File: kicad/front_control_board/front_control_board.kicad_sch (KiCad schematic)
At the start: 66 parts, among them J1 MAIN_BOARD, J2 DISPLAY, J3 PROG, J4 I2C, J5 AUX, J6 LED_OUT, Q1 DMN63D8LW, SW1 PEC11R-4215K-S0024, SW2 BTN1, SW3 BTN4, SW4 BTN2, SW5 BTN3, U1 ESP32-WROOM-32UE, U2 TCA9534

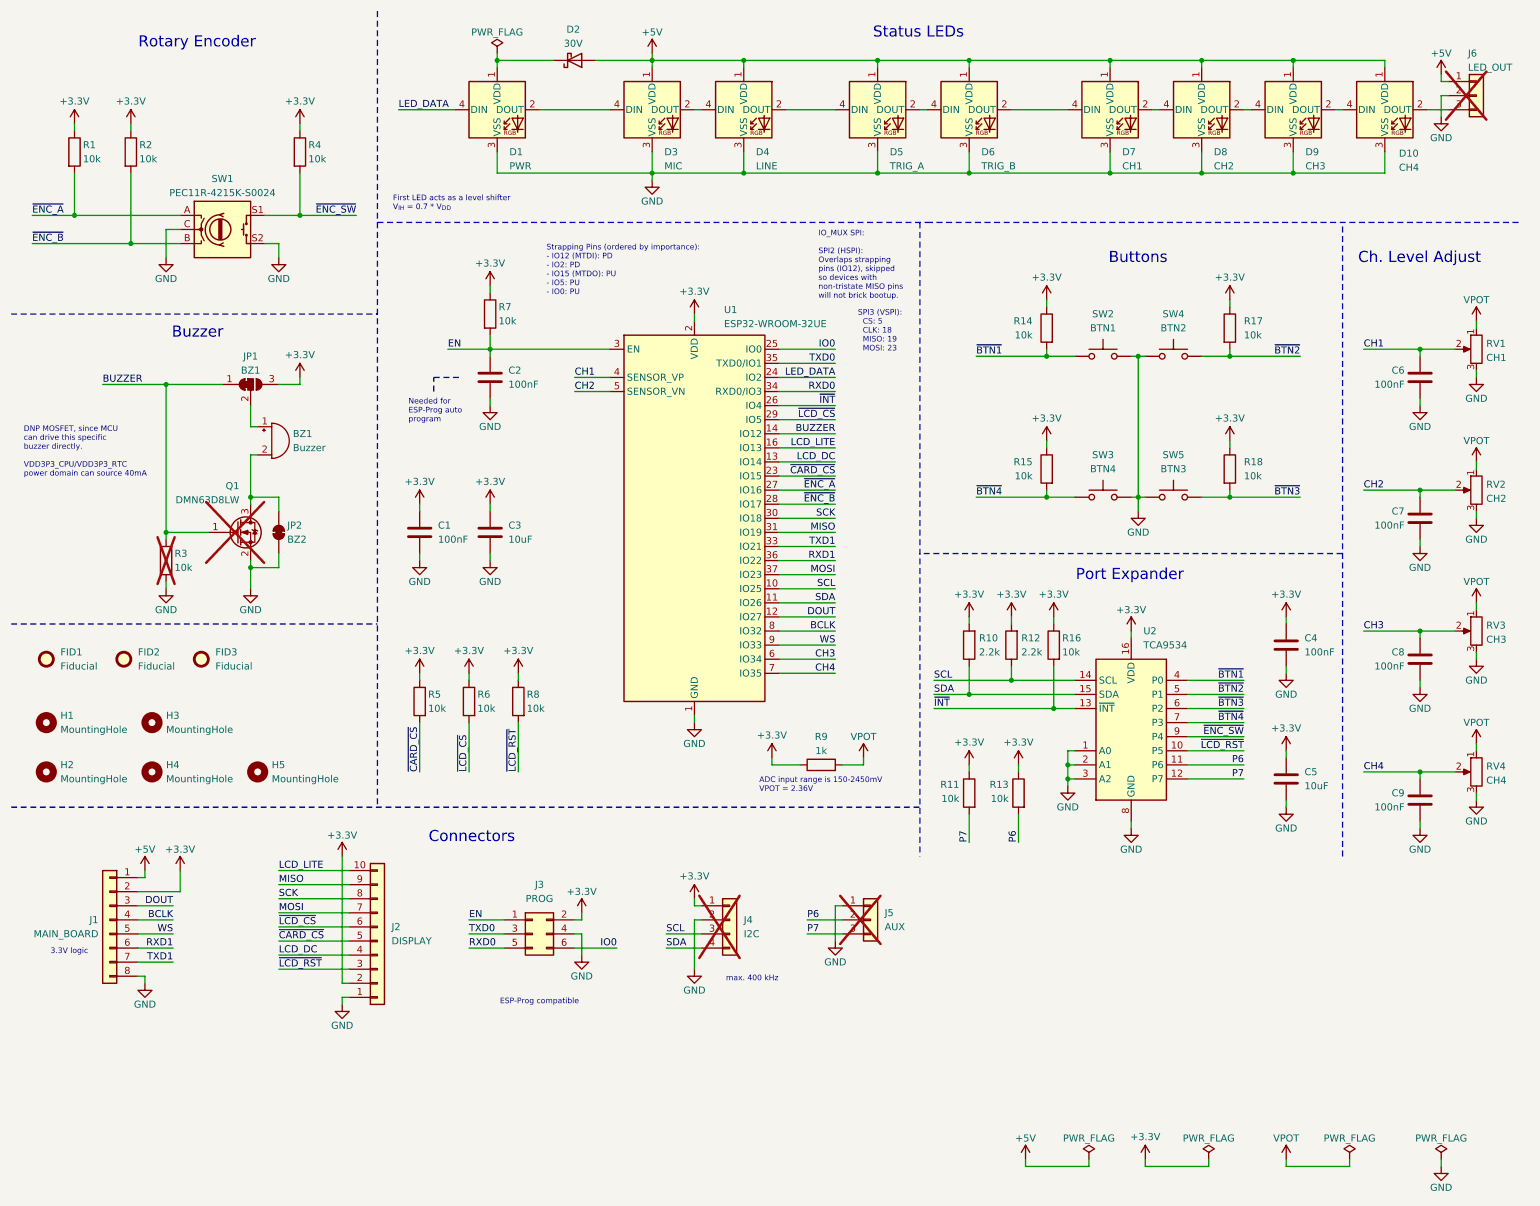
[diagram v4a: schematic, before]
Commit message: update BOM prioritizing basic parts
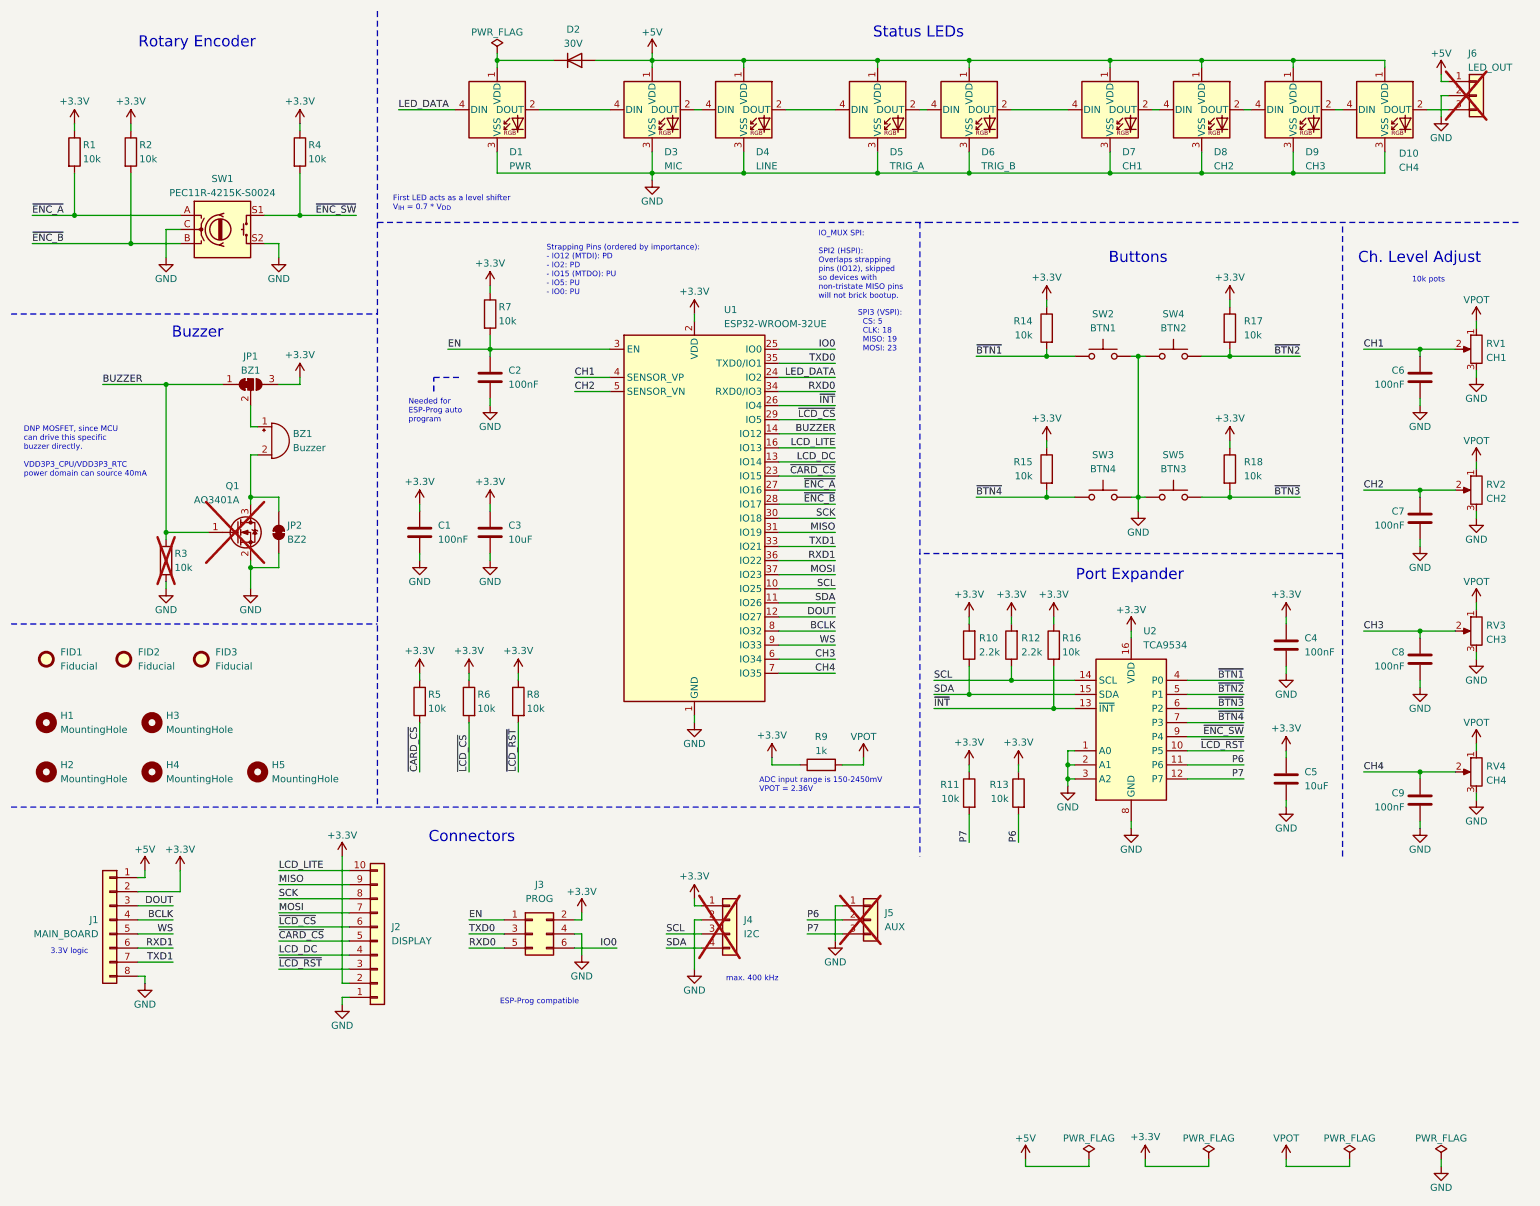
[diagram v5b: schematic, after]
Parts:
- BZ1: MOUSER 497-IE122303-1 -> (none); MPN IE122303-1 -> (none)
- C1, C2, C4, C6, C7, C8, C9: JLC (none) -> C14663; LCSC C1591 -> (none); MOUSER 187-CL10B104KB8NNNC -> (none); MPN CL10B104KB8NNNC -> (none)
- C3, C5: JLC (none) -> C96446; LCSC C96446 -> (none); MOUSER 187-CL10A106MA8NRNC -> (none); MPN CL10A106MA8NRNC -> (none)
- D1, D10, D3, D4, D5, D6, D7, D8, D9: JLC (none) -> C114586; LCSC C114586 -> (none); MOUSER 485-4684 -> (none); MPN WS2812B-B/W -> (none)
- D2: footprint Diode_SMD:D_SOD-523 -> Diode_SMD:D_SOD-323; symbol Device:D_Schottky -> Device:D; JLC (none) -> C2128; LCSC C232575 -> (none); MOUSER 863-RB520S30T5G -> (none); MPN RB520S30T5G -> (none)
- J1: footprint Connector_JST:JST_PH_B8B-PH-K_1x08_P2.00mm_Vertical -> Connector_JST:JST_XH_B8B-XH-A_1x08_P2.50mm_Vertical; LCSC (none) -> C7429638
- J2: LCSC (none) -> C492409
- J3: LCSC (none) -> C5372863
- J4: LCSC (none) -> C2691448
- J5, J6: LCSC (none) -> C2937625
- Q1: value DMN63D8LW -> AO3401A; footprint Package_TO_SOT_SMD:SOT-323_SC-70 -> Package_TO_SOT_SMD:SOT-23; JLC (none) -> C15127; LCSC C151057 -> (none); MOUSER 621-DMN63D8LW-7 -> (none); MPN DMN63D8LW-7 -> (none)
- R1, R11, R13, R14, R15, R16, R17, R18, R2, R3, R4, R5, R6, R7, R8: JLC (none) -> C25804; LCSC C25804 -> (none); MOUSER 603-RC0603FR-0710KL -> (none); MPN RC0603FR-0710KL -> (none)
- R10, R12: JLC (none) -> C4190; LCSC C4190 -> (none); MOUSER 603-RC0603FR-072K2L -> (none); MPN RC0603FR-072K2L -> (none)
- R9: JLC (none) -> C21190; LCSC C21190 -> (none); MOUSER 603-RC0603FR-071KL -> (none); MPN RC0603FR-071KL -> (none)
- RV1, RV2, RV3, RV4: LCSC (none) -> C6149573; MOUSER 652-PTV09A4020SB103 -> (none); MPN PTV09A-4020S-B103 -> (none)
- SW1: LCSC (none) -> C7275025; MOUSER 652-PEC11R-4215K-S24 -> (none); MPN PEC11R-4215K-S0024 -> (none)
- U1: JLC (none) -> C701346; LCSC C701346 -> (none); MOUSER 356-ESP32WRM32UE28UH -> (none); MPN ESP32-WROOM-32UE-N16 -> (none)
- U2: JLC (none) -> C783615
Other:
- note added: "10k pots"

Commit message: use tactile switches
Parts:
- SW2, SW3, SW4, SW5: footprint (none) -> Button_Switch_THT:SW_PUSH_6mm_H5mm; LCSC (none) -> C393938
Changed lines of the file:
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@@
 			)
 		)
-		(property "Datasheet" "~"
+		(property "Datasheet" "https://www.lcsc.com/datasheet/lcsc_datasheet_2404181051_BOURNS-PTV09A-4020S-B103_C6149573.pdf"
 			(at 276.86 149.86 0)
 			(effects
@@
 			)
 		)
-		(property "Footprint" ""
+		(property "Footprint" "Button_Switch_THT:SW_PUSH_6mm_H5mm"
 			(at 209.55 69.85 0)
 			(effects
@@
 			)
 		)
-		(property "Datasheet" ""
+		(property "Datasheet" "https://www.lcsc.com/datasheet/lcsc_datasheet_1912111437_SHOU-HAN-TS665CJ_C393938.pdf"
 			(at 209.55 69.85 0)
 			(effects
@@
 			)
 		)
-		(property "LCSC" ""
+		(property "LCSC" "C393938"
 			(at 209.55 74.93 0)
 			(effects
@@
 			)
 		)
-		(property "Footprint" ""
+		(property "Footprint" "Button_Switch_THT:SW_PUSH_6mm_H5mm"
 			(at 222.25 95.25 0)
 			(effects
@@
 			)
 		)
-		(property "Datasheet" ""
+		(property "Datasheet" "https://www.lcsc.com/datasheet/lcsc_datasheet_1912111437_SHOU-HAN-TS665CJ_C393938.pdf"
 			(at 222.25 95.25 0)
 			(effects
@@
 			)
 		)
-		(property "LCSC" ""
+		(property "LCSC" "C393938"
 			(at 222.25 100.33 0)
 			(effects
@@
 			)
 		)
-		(property "Footprint" ""
+		(property "Footprint" "Button_Switch_THT:SW_PUSH_6mm_H5mm"
 			(at 209.55 95.25 0)
 			(effects
@@
 			)
 		)
-		(property "Datasheet" ""
+		(property "Datasheet" "https://www.lcsc.com/datasheet/lcsc_datasheet_1912111437_SHOU-HAN-TS665CJ_C393938.pdf"
 			(at 209.55 95.25 0)
 			(effects
@@
 			)
 		)
-		(property "LCSC" ""
+		(property "LCSC" "C393938"
 			(at 209.55 100.33 0)
 			(effects
@@
 			)
 		)
-		(property "Datasheet" "~"
+		(property "Datasheet" "https://www.lcsc.com/datasheet/lcsc_datasheet_2404181051_BOURNS-PTV09A-4020S-B103_C6149573.pdf"
 			(at 276.86 73.66 0)
 			(effects
@@
 			)
 		)
-		(property "Datasheet" "~"
+		(property "Datasheet" "https://www.lcsc.com/datasheet/lcsc_datasheet_2404181051_BOURNS-PTV09A-4020S-B103_C6149573.pdf"
 			(at 276.86 124.46 0)
 			(effects
@@
 			)
 		)
-		(property "Footprint" ""
+		(property "Footprint" "Button_Switch_THT:SW_PUSH_6mm_H5mm"
 			(at 222.25 69.85 0)
 			(effects
@@
 			)
 		)
-		(property "Datasheet" ""
+		(property "Datasheet" "https://www.lcsc.com/datasheet/lcsc_datasheet_1912111437_SHOU-HAN-TS665CJ_C393938.pdf"
 			(at 222.25 69.85 0)
 			(effects
@@
 			)
 		)
-		(property "LCSC" ""
+		(property "LCSC" "C393938"
 			(at 222.25 74.93 0)
 			(effects
@@
 			)
 		)
-		(property "Datasheet" "~"
+		(property "Datasheet" "https://www.lcsc.com/datasheet/lcsc_datasheet_2404181051_BOURNS-PTV09A-4020S-B103_C6149573.pdf"
 			(at 276.86 99.06 0)
 			(effects
